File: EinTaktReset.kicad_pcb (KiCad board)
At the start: 2 copper layers, 50 parts, among them IC1 74LS624, J1 3PinTerminalBlocktg, J2 3PinTerminalBlocktg, J3 2PinTerminalBlocktg, J4 3PinTerminalBlocktg, J5 2PinTerminalBlocktg, P1 CONN_02X10, P4 CONN_02X10, SW1 SPST, SW10 SPST, SW11 SPST, SW12 SPST, SW13 SPST, SW2 SWITCH_INV, SW3 SPST, SW4 SPST, SW5 SPST, SW6 SWITCH_INV, SW7 SPST, SW8 SPST, SW9 SPST, U1 74LS132, U2 74540En, U3 74HCT541_PWR, U4 74LS32, U5 74LS00, U6 74LS132

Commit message: todo aktualisiert und gelayoutet
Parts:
- added D3: D, LEDs:LED_D1.8mm_W1.8mm_H2.4mm_Horizontal_O1.27mm_Z4.9mm, F.Cu at (245.1, -12.7)
- added R14: 4,7k, Resistors_ThroughHole:R_Axial_DIN0207_L6.3mm_D2.5mm_P10.16mm_Horizontal, F.Cu at (137.2, 10.2)
- added R15: 4,7k, Resistors_ThroughHole:R_Axial_DIN0207_L6.3mm_D2.5mm_P10.16mm_Horizontal, F.Cu at (138.4, 16.5)
- added R16: 4,7k, Resistors_ThroughHole:R_Axial_DIN0207_L6.3mm_D2.5mm_P10.16mm_Horizontal, F.Cu at (151.1, 3.81)
- added R17: 10k, Resistors_ThroughHole:R_Axial_DIN0207_L6.3mm_D2.5mm_P10.16mm_Horizontal, F.Cu at (29.2, 105.4)
- moved IC1 324.1 mm to (35.6, 104.1), turned to 90 degrees
- moved J3 270.9 mm to (147.3, -19.1)
- moved J4 245.7 mm to (171.4, -20.3)
- moved J5 243.0 mm to (190.5, -20.3)
- moved R1 205.0 mm to (26.7, 172.7)
- moved U4 169.0 mm to (64.8, 104.1), turned to 90 degrees
- moved R3 151.8 mm to (91.4, 167.6)
- moved SW3 151.8 mm to (221.0, -22.9)
- moved C2 133.1 mm to (224.8, -10.2)
- moved SW4 123.1 mm to (246.4, -24.1)
- moved U5 90.7 mm to (47.0, 133.3), turned to 90 degrees
- moved D1 3.81 mm to (27.9, 166.4)

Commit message: pcb gelayoutet, footprint für capacitors geadded, 74ls32 teile zugeordnet, todo überarbeitet
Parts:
- removed U6: 74LS132, Housings_DIP:DIP-14_W7.62mm_Socket_LongPads
- added C6: 100n, Capacitors_ThroughHole:C_Disc_D10.0mm_W2.5mm_P5.00mm, F.Cu at (73.7, 116.8)
- added C7: 100n, Capacitors_ThroughHole:C_Disc_D10.0mm_W2.5mm_P5.00mm, F.Cu at (49.5, 139.7)
- added C8: 100n, Capacitors_ThroughHole:C_Disc_D10.0mm_W2.5mm_P5.00mm, F.Cu at (38.1, 177.8)
- added C9: 100n, Capacitors_ThroughHole:C_Disc_D10.0mm_W2.5mm_P5.00mm, F.Cu at (29.2, 55.9)
- moved SW4 279.8 mm to (17.8, 137.2), turned to 90 degrees
- moved R16 227.5 mm to (-17.8, 156.2), turned to 90 degrees
- moved C3 224.1 mm to (19.1, 118.1), turned to 270 degrees
- moved C4 223.5 mm to (30.5, 121.9), turned to 90 degrees
- moved C2 222.0 mm to (106.7, 177.8), turned to 270 degrees
- moved D3 214.5 mm to (33.0, 19.1)
- moved RV1 208.6 mm to (29.2, 132.1), turned to 270 degrees
- moved SW3 201.9 mm to (106.7, 143.5), turned to 180 degrees
- moved R15 200.2 mm to (-20.3, 138.4)
- moved R14 198.2 mm to (-19.1, 132.1)
- moved DROT1 193.4 mm to (69.8, 95.2), turned to 180 degrees
- moved C5 188.8 mm to (39.4, 120.7), turned to 90 degrees
- moved R10 182.7 mm to (43.2, 134.6)
- moved R9 161.6 mm to (100.3, 165.1)
- moved R13 160.8 mm to (101.6, 158.8)
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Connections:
- U4 pad 1: CLK -> Net-(U3-Pad1)
- U4 pad 10: Net-(U1-Pad10) -> CLK
- U4 pad 11: (no net) -> CLK
- U4 pad 12: (no net) -> Net-(U4-Pad12)
- U4 pad 13: (no net) -> Net-(U1-Pad10)
- U4 pad 2: CLK -> Net-(U3-Pad1)
- U4 pad 3: Net-(R4-Pad1) -> Net-(R7-Pad1)
- U4 pad 4: Net-(U3-Pad1) -> auto
- U4 pad 5: Net-(U3-Pad1) -> enDEC
- U4 pad 6: Net-(R7-Pad1) -> enSTW
- U4 pad 8: CLK -> Net-(R4-Pad1)
- U4 pad 9: Net-(U4-Pad9) -> CLK
- U5 pad 6: Net-(U4-Pad9) -> Net-(U4-Pad12)

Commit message: grobplazierung fertiggestellt, feinplatzierung angefangen
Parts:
- added REF**: EuroBoard160mmX100mm, EuroBoard_Outline:EuroBoard160mmX100mm, F.Cu at (111.8, 198.1)
- D1: footprint Diodes_ThroughHole:D_DO-35_SOD27_P7.62mm_Horizontal -> Diodes_ThroughHole:D_DO-35_SOD27_P10.16mm_Horizontal
- D3: footprint LEDs:LED_D1.8mm_W1.8mm_H2.4mm_Horizontal_O1.27mm_Z4.9mm -> Diodes_ThroughHole:D_DO-35_SOD27_P10.16mm_Horizontal
- moved R2 223.3 mm to (21.6, 175.3), turned to 270 degrees
- moved J5 223.1 mm to (104.1, 185.4), turned to 270 degrees
- moved R6 201.7 mm to (63.5, 190.5), turned to 90 degrees
- moved J4 200.3 mm to (118.1, 172.7), turned to 90 degrees
- moved R5 173.2 mm to (80.0, 193.0)
- moved J3 133.5 mm to (19.1, 17.8)
- moved J2 86.0 mm to (127.0, 123.2), turned to 270 degrees
- moved J1 84.4 mm to (118.1, 143.5), turned to 270 degrees
- moved R15 64.9 mm to (35.6, 171.4), turned to 180 degrees
- moved R14 56.9 mm to (25.4, 167.6)
- moved R16 38.1 mm to (15.2, 175.3)
- moved R11 18.2 mm to (49.5, 147.3)
- moved R10 16.9 mm to (39.4, 151.1)
- moved U5 16.6 mm to (41.9, 167.6)
- moved C7 16.1 mm to (44.5, 154.9)
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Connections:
- R16 pad 2: Net-(R16-Pad2) -> Net-(IC1-Pad5)
- U1 pad 13: Net-(R15-Pad1) -> Net-(R14-Pad2)
- U1 pad 9: Net-(R14-Pad2) -> Net-(R15-Pad1)
- U2 pad 11: clrPC -> Net-(U2-Pad11)
- U2 pad 12: clrAkku -> Net-(U2-Pad12)
- U2 pad 13: loadIR -> Net-(R15-Pad1)
- U2 pad 14: enAkku -> clrPC
- U2 pad 15: clrMPC -> clrAkku
- U2 pad 16: Net-(U2-Pad16) -> loadIR
- U2 pad 17: Net-(U2-Pad17) -> enAkku
- U2 pad 18: Net-(R15-Pad1) -> clrMPC
- U2 pad 2: Net-(U2-Pad17) -> Net-(R6-Pad1)
- U2 pad 3: Net-(U2-Pad16) -> Net-(R6-Pad1)
- U2 pad 4: Net-(C2-Pad1) -> Net-(R6-Pad1)
- U2 pad 5: Net-(R6-Pad1) -> Net-(R5-Pad1)
- U2 pad 6: Net-(R6-Pad1) -> Net-(R5-Pad1)
- U2 pad 7: Net-(R6-Pad1) -> Net-(U2-Pad12)
- U2 pad 8: Net-(R5-Pad1) -> Net-(U2-Pad11)
- U2 pad 9: Net-(R5-Pad1) -> Net-(C2-Pad1)
- U4 pad 12: Net-(U4-Pad12) -> Net-(U1-Pad12)
- U4 pad 13: Net-(U1-Pad10) -> Net-(U4-Pad13)
- U4 pad 2: Net-(U3-Pad1) -> Net-(U4-Pad2)
- U4 pad 4: auto -> enDEC
- U4 pad 5: enDEC -> auto
- U5 pad 1: Net-(IC1-Pad8) -> Net-(U1-Pad6)
- U5 pad 12: en-ln1 -> en-ln2
- U5 pad 13: en-ln2 -> en-ln1
- U5 pad 2: Net-(U1-Pad6) -> Net-(IC1-Pad8)
- U5 pad 6: Net-(U4-Pad12) -> Net-(U4-Pad13)
- U5 pad 8: Net-(U3-Pad1) -> Net-(U4-Pad2)
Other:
- board outline added: 100 x 160 mm

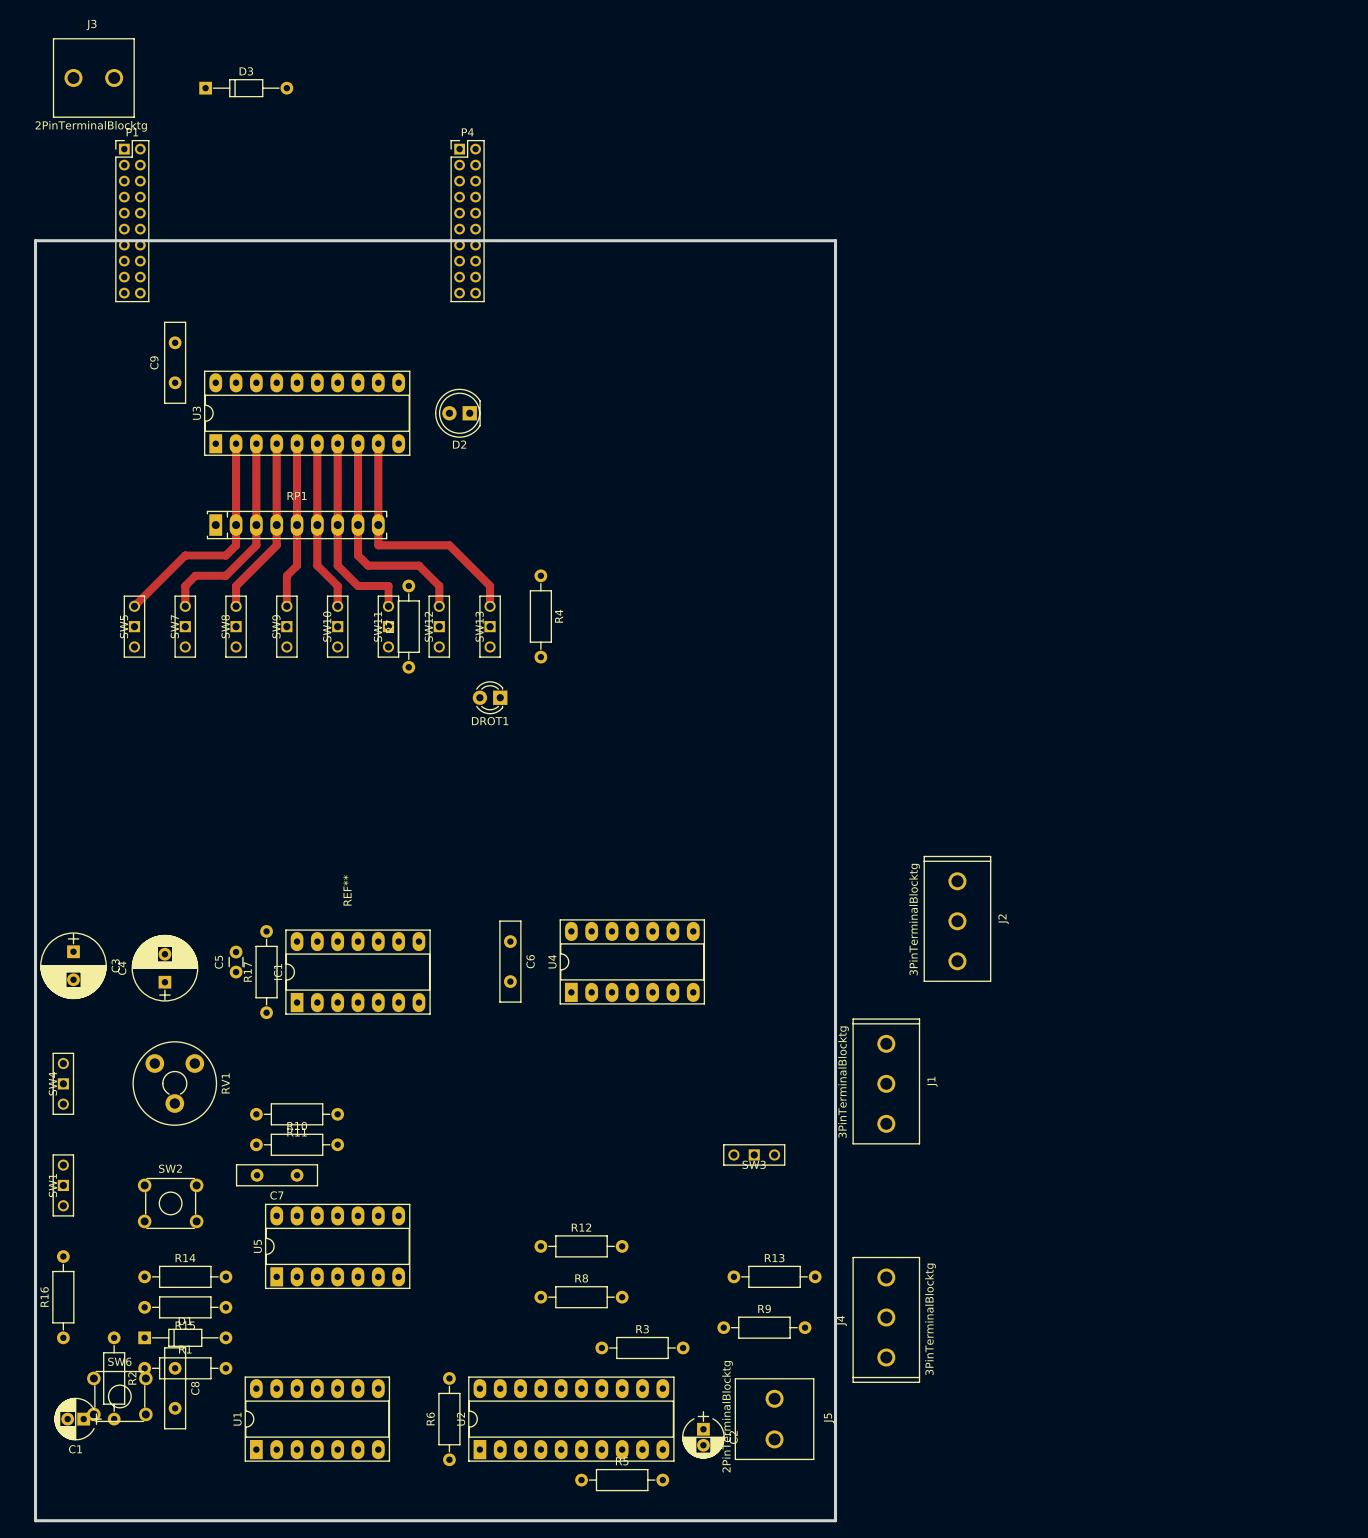
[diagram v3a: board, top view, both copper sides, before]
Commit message: Library für switches geadded
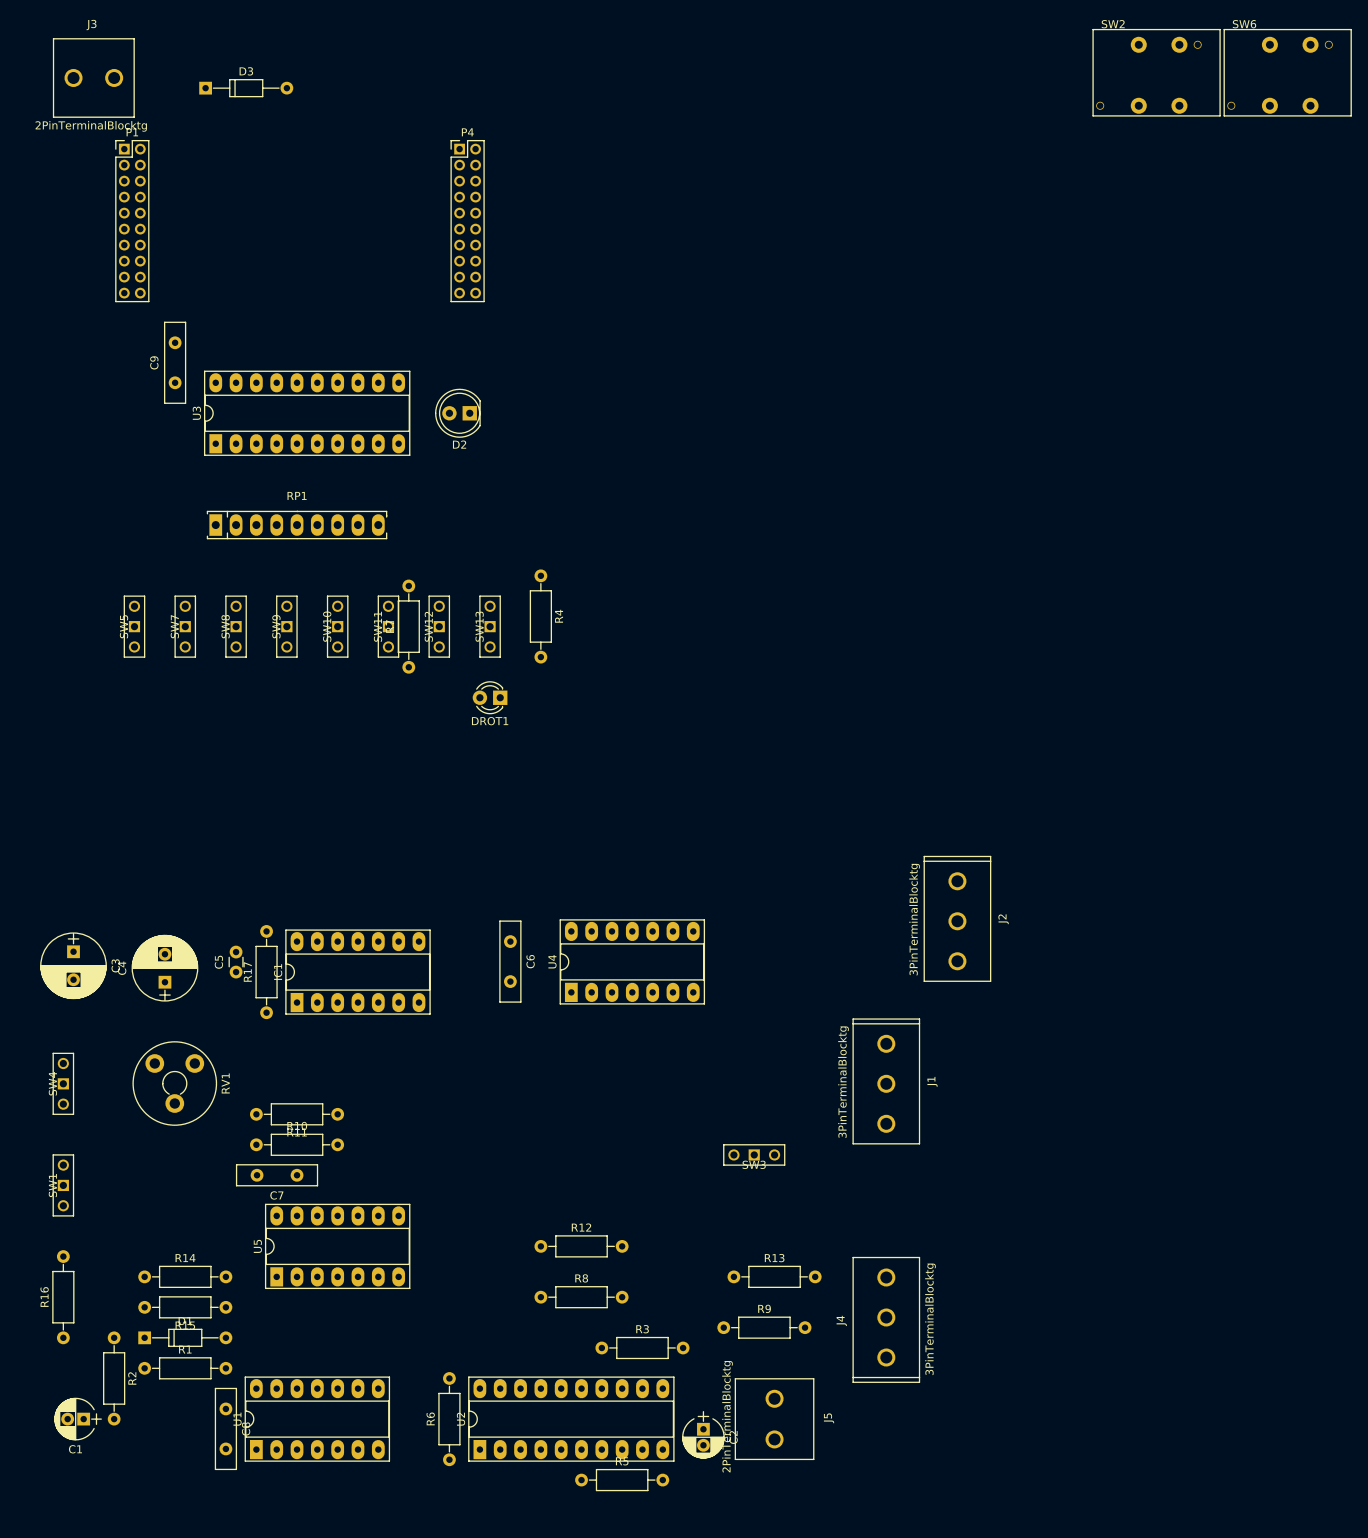
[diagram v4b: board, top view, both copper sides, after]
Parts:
- removed REF**: EuroBoard160mmX100mm, EuroBoard_Outline:EuroBoard160mmX100mm
- SW2, SW6: footprint Buttons_Switches_ThroughHole:SW_TH_Tactile_Omron_B3F-10xx -> tg_foodprint:SW_PUSH_LCD_E3_SAxxxx_tg
- moved SW6 225.7 mm to (171.1, 13.6)
- moved SW2 192.5 mm to (154.7, 13.6)
- moved C8 8.13 mm to (35.6, 184.2)
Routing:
- net Net-(RP1-Pad9): track 31.3 -> 0.00 mm
- net Net-(RP1-Pad2): track 28.6 -> 0.00 mm
- net Net-(RP1-Pad8): track 28.2 -> 0.00 mm
- net Net-(RP1-Pad3): track 26.2 -> 0.00 mm
- net Net-(RP1-Pad7): track 25.2 -> 0.00 mm
- net Net-(RP1-Pad4): track 22.4 -> 0.00 mm
- net Net-(RP1-Pad6): track 21.4 -> 0.00 mm
- net Net-(RP1-Pad5): track 20.8 -> 0.00 mm
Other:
- board outline removed
